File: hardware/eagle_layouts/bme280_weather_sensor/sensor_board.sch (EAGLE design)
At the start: 10 parts, among them CN1 1X4-CLEANBIG, IC1 REG1117, T1 ZXMD63N03XSOT-363, U1 BME280

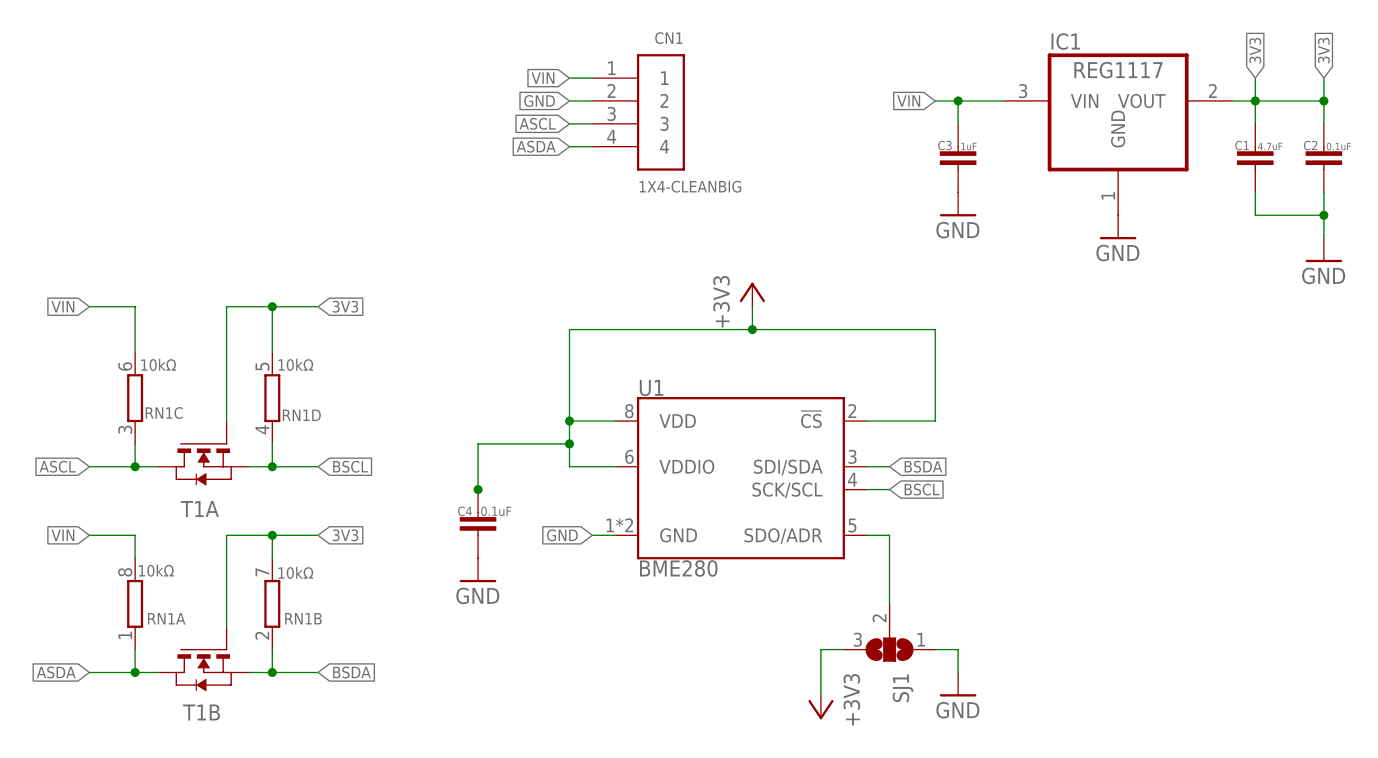
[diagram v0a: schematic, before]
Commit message: Starting board layout for BME280 breakout
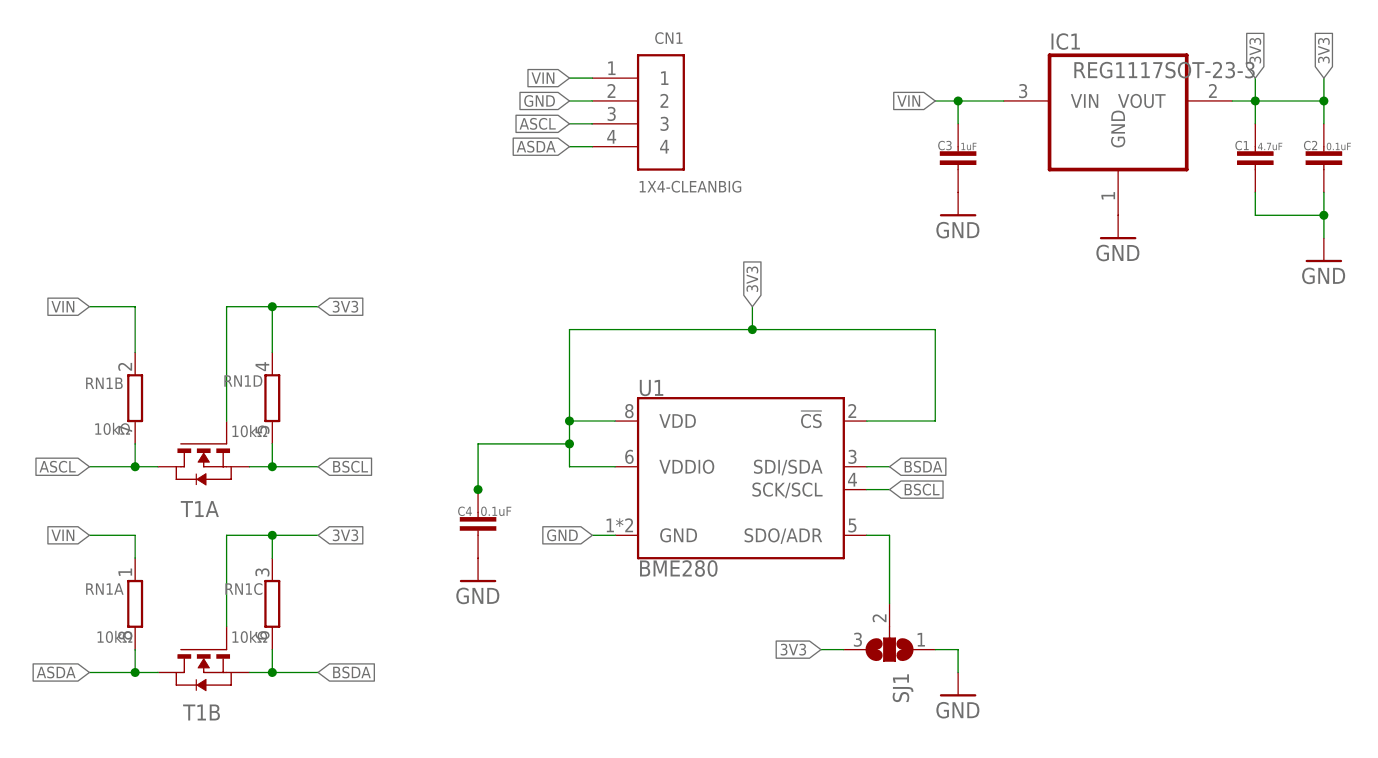
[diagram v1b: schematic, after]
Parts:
- IC1: value REG1117 -> REG1117SOT-23-3; device burr-brown:REG1117 -> sensor_board:REG1117SOT-23-3
- T1: device zetex:ZXMD63N03XSOT-363 -> sensor_board:ZXMD63N03XSOT-363
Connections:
- removed net +3V3: C4.1, SJ1.3, U1.!CS, U1.VDD, U1.VDDIO
- net 3V3: now also C4.1, RN1C.1, RN1D.1, SJ1.3, U1.!CS, U1.VDD, U1.VDDIO; no longer RN1B.2, RN1D.2
- net ASCL: now also RN1B.2; no longer RN1C.1
- net ASDA: now also RN1A.2; no longer RN1A.1
- net BSCL: now also RN1D.2; no longer RN1D.1
- net BSDA: now also RN1C.2; no longer RN1B.1
- net VIN: now also RN1A.1, RN1B.1; no longer RN1A.2, RN1C.2
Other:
- moved on the sheet: RN1A, RN1B, RN1C, RN1D
